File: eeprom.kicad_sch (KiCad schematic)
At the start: 4 parts

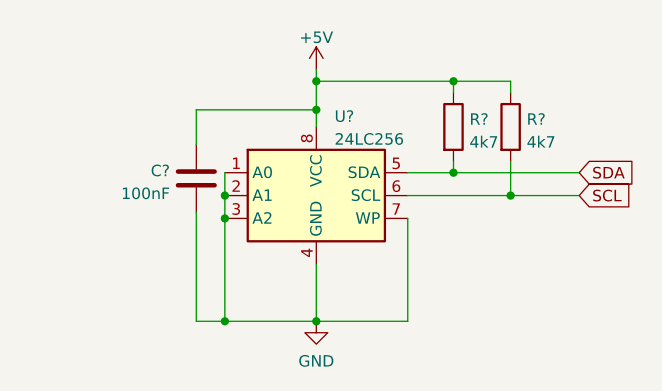
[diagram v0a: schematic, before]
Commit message: added hierarchial labels to some schematics
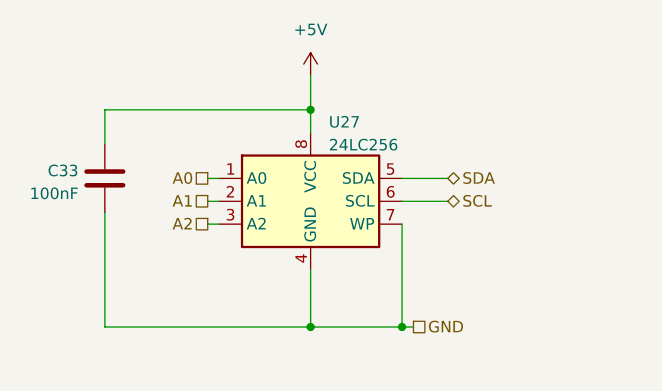
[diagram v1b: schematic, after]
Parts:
- removed R? (x2): 4k7, Resistor_SMD:R_0603_1608Metric, symbol Device:R
- gave numbers to parts that had none: 2
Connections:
- net GND: no longer U27.1 (A0), U27.2 (A1), U27.3 (A2)
- new net A0: U27.1 (A0)
- new net A1: U27.2 (A1)
- new net A2: U27.3 (A2)
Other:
- moved on the sheet: C33, U27
